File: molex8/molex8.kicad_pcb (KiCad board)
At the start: 2 copper layers, 43 x 40 mm, 7 parts, among them J1 Conn_01x04, J2 Conn_02x04_Counter_Clockwise, J3 Conn_01x04

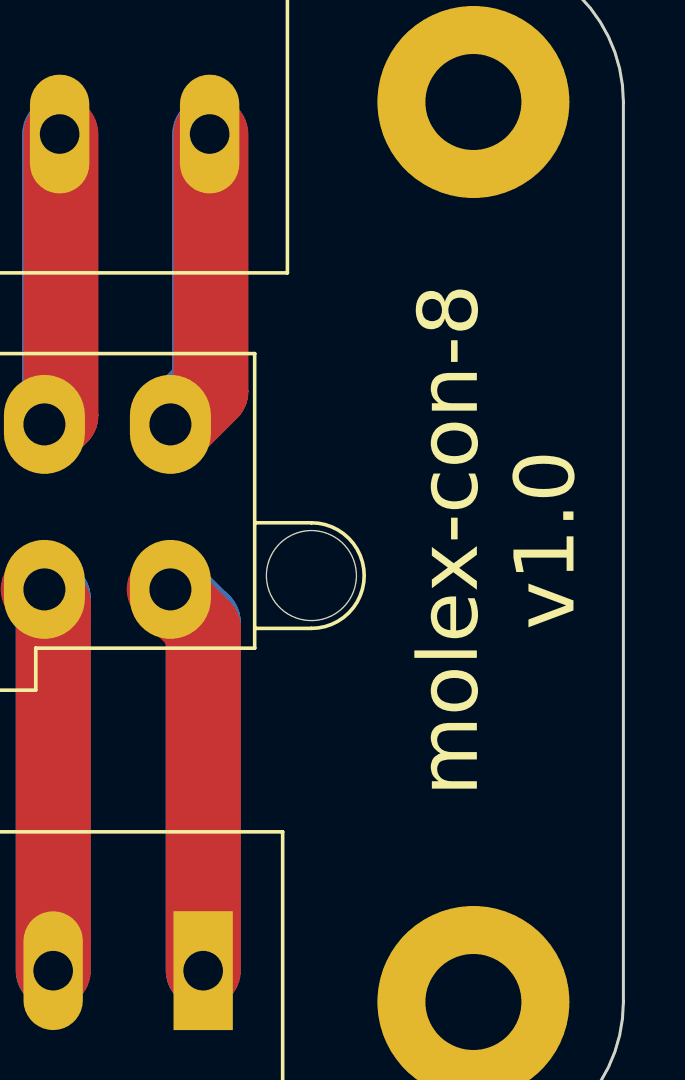
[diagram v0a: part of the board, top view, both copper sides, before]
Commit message: Update silkscreen.
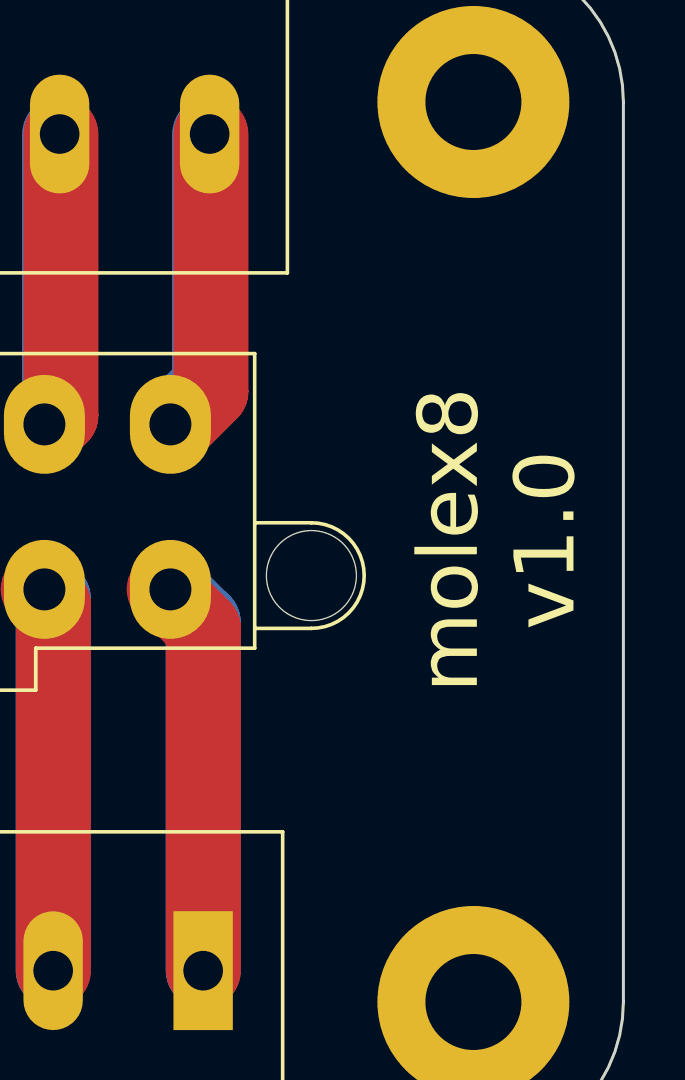
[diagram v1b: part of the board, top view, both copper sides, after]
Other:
- board text added: "molex8 v1.0"
- board text removed: "molex-con-8 v1.0"
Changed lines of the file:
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@@
   (gr_arc (start 85 116) (mid 81.464466 114.535534) (end 80 111) (layer "Edge.Cuts") (width 0.1))
   (gr_arc (start 123 111) (mid 121.535534 114.535534) (end 118 116) (layer "Edge.Cuts") (width 0.1))
-  (gr_text "molex-con-8\nv1.0" (at 118.8 95.6 90) (layer "F.SilkS")
+  (gr_text "molex8\nv1.0" (at 118.8 95.6 90) (layer "F.SilkS")
     (effects (font (size 2 2) (thickness 0.2)))
   )

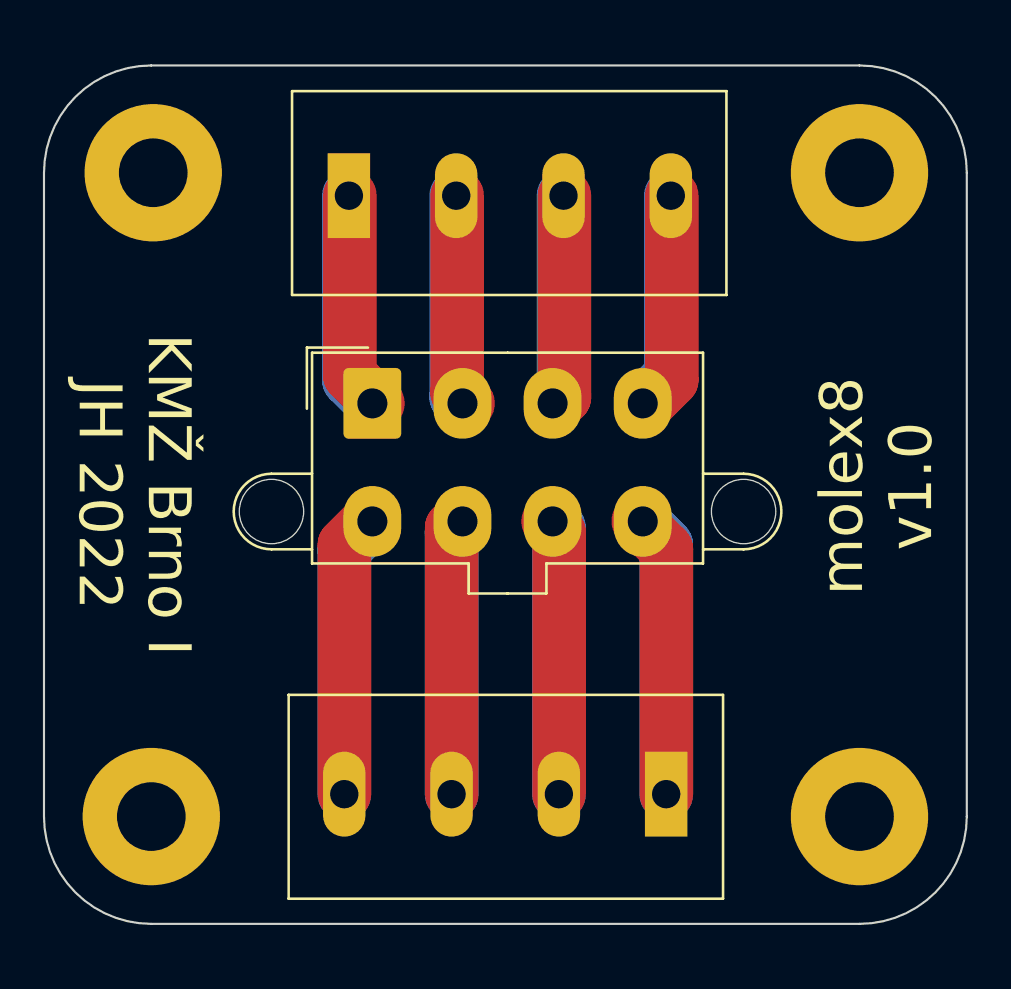
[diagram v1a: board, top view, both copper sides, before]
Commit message: Standardize dimensions to 42x42 mm.
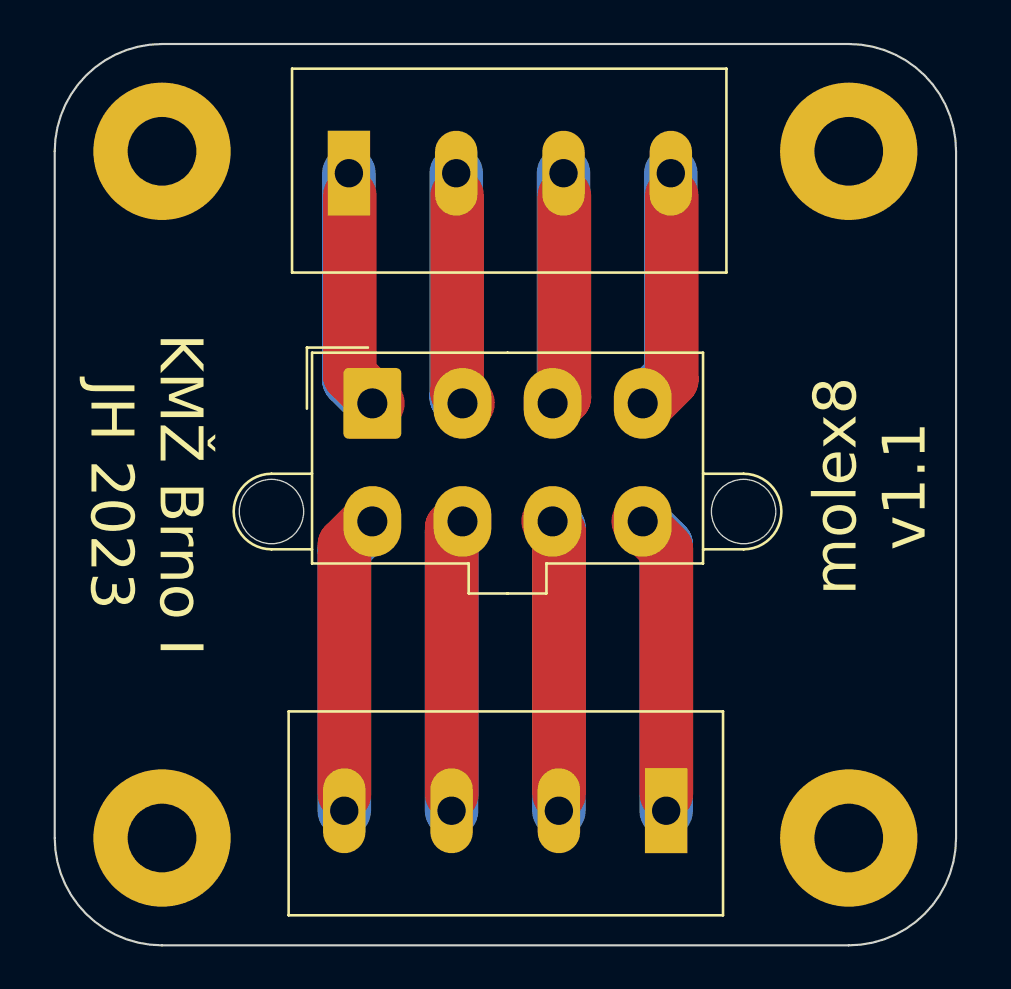
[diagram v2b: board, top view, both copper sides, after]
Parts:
- moved H2 1.12 mm to (117.5, 112.0)
- moved H3 1.12 mm to (85.5, 112.0)
- moved H4 1.12 mm to (117.5, 80.0)
- moved H1 1.08 mm to (85.5, 80.0)
- moved J1 1.05 mm to (101.6, 81.2)
- moved J3 0.77 mm to (101.6, 110.5)
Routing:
- net Net-(J1-Pad4): track 20.4 -> 21.4 mm
- net Net-(J1-Pad3): track 19.7 -> 20.7 mm
- net Net-(J1-Pad2): track 19.7 -> 20.7 mm
- net Net-(J1-Pad1): track 20.4 -> 21.4 mm
- net Net-(J2-Pad8): track 26.4 -> 27.2 mm
- net Net-(J2-Pad7): track 25.8 -> 26.5 mm
- net Net-(J2-Pad6): track 25.8 -> 26.5 mm
- net Net-(J2-Pad5): track 26.4 -> 27.2 mm
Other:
- board size 43 x 40 mm -> 42 x 42 mm
- board text added: "KMŽ Brno I JH 2023"
- board text added: "molex8 v1.1"
- board text removed: "KMŽ Brno I JH 2022"
- board text removed: "molex8 v1.0"
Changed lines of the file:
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@@
   )
   (footprint "MountingHole:MountingHole_3.2mm_M3_Pad" (layer "F.Cu")
-    (at 85.09 81)
+    (at 85.5 80)
     (descr "Mounting Hole 3.2mm, M3")
     (tags "mounting hole 3.2mm m3")
@@
   )
   (footprint "TerminalBlock_Euroclamp:MVE252-5-V-2x" (layer "F.Cu")
-    (at 101.6 82.296)
+    (at 101.6 81.25)
     (property "Sheetfile" "molex-con.kicad_sch")
     (property "Sheetname" "")
@@
   )
   (footprint "TerminalBlock_Euroclamp:MVE252-5-V-2x" (layer "F.Cu")
-    (at 101.6 109.728 180)
+    (at 101.6 110.5 180)
     (property "Sheetfile" "molex-con.kicad_sch")
     (property "Sheetname" "")
@@
   )
   (footprint "MountingHole:MountingHole_3.2mm_M3_Pad" (layer "F.Cu")
-    (at 118 81)
+    (at 117.5 80)
     (descr "Mounting Hole 3.2mm, M3")
     (tags "mounting hole 3.2mm m3")
@@
   )
   (footprint "MountingHole:MountingHole_3.2mm_M3_Pad" (layer "F.Cu")
-    (at 118 111)
+    (at 117.5 112)
     (descr "Mounting Hole 3.2mm, M3")
     (tags "mounting hole 3.2mm m3")
@@
   )
   (footprint "MountingHole:MountingHole_3.2mm_M3_Pad" (layer "F.Cu")
-    (at 85 111)
+    (at 85.5 112)
     (descr "Mounting Hole 3.2mm, M3")
     (tags "mounting hole 3.2mm m3")
@@
   (gr_line (start 109 110) (end 109 98.25) (layer "B.Mask") (width 2.5))
   (gr_line (start 94 98.75) (end 95.25 97.25) (layer "B.Mask") (width 2.5))
-  (gr_arc (start 118 76) (mid 121.535534 77.464466) (end 123 81) (layer "Edge.Cuts") (width 0.1))
-  (gr_arc (start 80 81) (mid 81.464466 77.464466) (end 85 76) (layer "Edge.Cuts") (width 0.1))
-  (gr_line (start 118 116) (end 85 116) (layer "Edge.Cuts") (width 0.1))
-  (gr_line (start 80 111) (end 80 81) (layer "Edge.Cuts") (width 0.1))
-  (gr_line (start 85 76) (end 118 76) (layer "Edge.Cuts") (width 0.1))
-  (gr_line (start 123 81) (end 123 111) (layer "Edge.Cuts") (width 0.1))
-  (gr_arc (start 85 116) (mid 81.464466 114.535534) (end 80 111) (layer "Edge.Cuts") (width 0.1))
-  (gr_arc (start 123 111) (mid 121.535534 114.535534) (end 118 116) (layer "Edge.Cuts") (width 0.1))
-  (gr_text "molex8\nv1.0" (at 118.8 95.6 90) (layer "F.SilkS")
+  (gr_arc (start 117.5 75) (mid 121.035534 76.464466) (end 122.5 80) (layer "Edge.Cuts") (width 0.1))
+  (gr_arc (start 80.5 80) (mid 81.964466 76.464466) (end 85.5 75) (layer "Edge.Cuts") (width 0.1))
+  (gr_line (start 117.5 117) (end 85.5 117) (layer "Edge.Cuts") (width 0.1))
+  (gr_line (start 80.5 112) (end 80.5 80) (layer "Edge.Cuts") (width 0.1))
+  (gr_line (start 85.5 75) (end 117.5 75) (layer "Edge.Cuts") (width 0.1))
+  (gr_line (start 122.5 80) (end 122.5 112) (layer "Edge.Cuts") (width 0.1))
+  (gr_arc (start 85.5 117) (mid 81.964466 115.535534) (end 80.5 112) (layer "Edge.Cuts") (width 0.1))
+  (gr_arc (start 122.5 112) (mid 121.035534 115.535534) (end 117.5 117) (layer "Edge.Cuts") (width 0.1))
+  (gr_text "molex8\nv1.1" (at 118.5 95.6 90) (layer "F.SilkS")
     (effects (font (size 2 2) (thickness 0.2)))
   )
-  (gr_text "KMŽ Brno I\nJH 2022" (at 84.2 96 270) (layer "F.SilkS")
+  (gr_text "KMŽ Brno I\nJH 2023" (at 84.75 96 270) (layer "F.SilkS")
     (effects (font (size 2 2) (thickness 0.2)))
   )
@@
   (segment (start 94.25 90.435) (end 95.558 91.743) (width 2.5) (layer "F.Cu") (net 1))
   (segment (start 94.25 82.065) (end 94.25 90.435) (width 2.5) (layer "F.Cu") (net 1))
-  (segment (start 94.208 82.068) (end 94.208 90.654) (width 2.5) (layer "B.Cu") (net 1))
+  (segment (start 94.208 81.022) (end 94.208 90.654) (width 2.5) (layer "B.Cu") (net 1))
   (segment (start 94.208 90.654) (end 95.3 91.746) (width 2.5) (layer "B.Cu") (net 1))
   (segment (start 99.25 82.065) (end 99.25 91.235) (width 2.5) (layer "F.Cu") (net 2))
   (segment (start 99.25 91.235) (end 99.758 91.743) (width 2.5) (layer "F.Cu") (net 2))
-  (segment (start 99.208 82.068) (end 99.208 91.454) (width 2.5) (layer "B.Cu") (net 2))
+  (segment (start 99.208 81.022) (end 99.208 91.454) (width 2.5) (layer "B.Cu") (net 2))
   (segment (start 99.208 91.454) (end 99.5 91.746) (width 2.5) (layer "B.Cu") (net 2))
   (segment (start 104.25 91.451) (end 103.958 91.743) (width 2.5) (layer "F.Cu") (net 3))
   (segment (start 104.25 82.065) (end 104.25 91.451) (width 2.5) (layer "F.Cu") (net 3))
   (segment (start 104.208 91.238) (end 103.7 91.746) (width 2.5) (layer "B.Cu") (net 3))
-  (segment (start 104.208 82.068) (end 104.208 91.238) (width 2.5) (layer "B.Cu") (net 3))
+  (segment (start 104.208 81.022) (end 104.208 91.238) (width 2.5) (layer "B.Cu") (net 3))
   (segment (start 109.25 82.065) (end 109.25 90.651) (width 2.5) (layer "F.Cu") (net 4))
   (segment (start 109.25 90.651) (end 108.158 91.743) (width 2.5) (layer "F.Cu") (net 4))
   (segment (start 109.208 90.438) (end 107.9 91.746) (width 2.5) (layer "B.Cu") (net 4))
-  (segment (start 109.208 82.068) (end 109.208 90.438) (width 2.5) (layer "B.Cu") (net 4))
+  (segment (start 109.208 81.022) (end 109.208 90.438) (width 2.5) (layer "B.Cu") (net 4))
   (segment (start 94 109.951) (end 94 98.333) (width 2.5) (layer "F.Cu") (net 5))
   (segment (start 94 98.333) (end 95.092 97.241) (width 2.5) (layer "F.Cu") (net 5))
   (segment (start 93.992 98.554) (end 95.3 97.246) (width 2.5) (layer "B.Cu") (net 5))
-  (segment (start 93.992 109.956) (end 93.992 98.554) (width 2.5) (layer "B.Cu") (net 5))
+  (segment (start 93.992 110.728) (end 93.992 98.554) (width 2.5) (layer "B.Cu") (net 5))
   (segment (start 99 109.951) (end 99 97.533) (width 2.5) (layer "F.Cu") (net 6))
   (segment (start 99 97.533) (end 99.292 97.241) (width 2.5) (layer "F.Cu") (net 6))
+  (segment (start 98.992 110.728) (end 98.992 97.754) (width 2.5) (layer "B.Cu") (net 6))
   (segment (start 98.992 97.754) (end 99.5 97.246) (width 2.5) (layer "B.Cu") (net 6))
-  (segment (start 98.992 109.956) (end 98.992 97.754) (width 2.5) (layer "B.Cu") (net 6))
   (segment (start 104 97.749) (end 103.492 97.241) (width 2.5) (layer "F.Cu") (net 7))
   (segment (start 104 109.951) (end 104 97.749) (width 2.5) (layer "F.Cu") (net 7))
-  (segment (start 103.992 109.956) (end 103.992 97.538) (width 2.5) (layer "B.Cu") (net 7))
   (segment (start 103.992 97.538) (end 103.7 97.246) (width 2.5) (layer "B.Cu") (net 7))
+  (segment (start 103.992 110.728) (end 103.992 97.538) (width 2.5) (layer "B.Cu") (net 7))
   (segment (start 109 109.951) (end 109 98.549) (width 2.5) (layer "F.Cu") (net 8))
   (segment (start 109 98.549) (end 107.692 97.241) (width 2.5) (layer "F.Cu") (net 8))
-  (segment (start 108.992 109.956) (end 108.992 98.338) (width 2.5) (layer "B.Cu") (net 8))
+  (segment (start 108.992 110.728) (end 108.992 98.338) (width 2.5) (layer "B.Cu") (net 8))
   (segment (start 108.992 98.338) (end 107.9 97.246) (width 2.5) (layer "B.Cu") (net 8))
 )

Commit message: Use screw terminal symbols, use MVE25-5-V as values.
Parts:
- H1, H2, H3, H4: value MountingHole -> MountingHole-3.2mm
- J1, J3: value Conn_01x04 -> 2xMVE252-5-V
- J2: value Conn_02x04_Counter_Clockwise -> TME 39281083 MOLEX
